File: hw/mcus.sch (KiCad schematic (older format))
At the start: 45 parts, among them P14 CONN_2, P18 CONN_1, SW2 EVQP7A01K, U10 MICRON N25Q032A13ESC40G, U13 MPU-9250, U7 STM32F427VIT6, U8 STM32F303CC, U9 MS5611, X1 8MHz, X2 8MHz

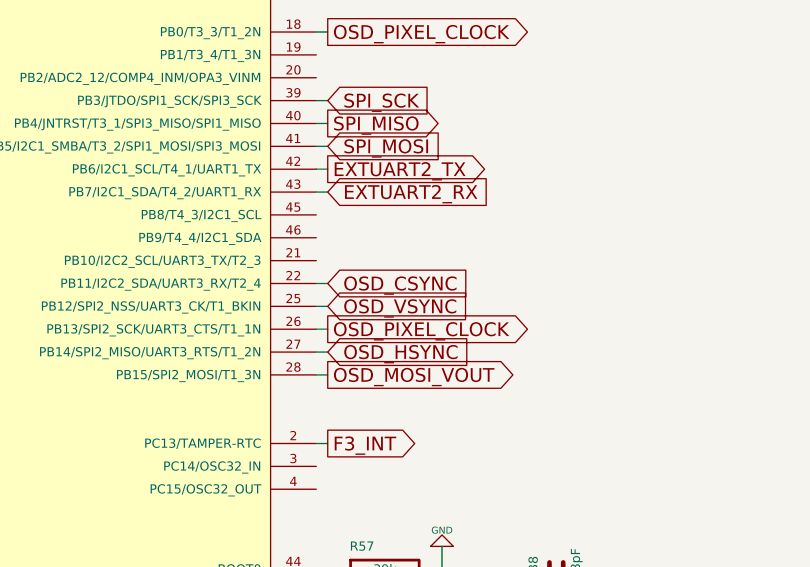
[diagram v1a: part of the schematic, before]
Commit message: hw: add chroma filter to sync separator, removed unused CSYNC signal
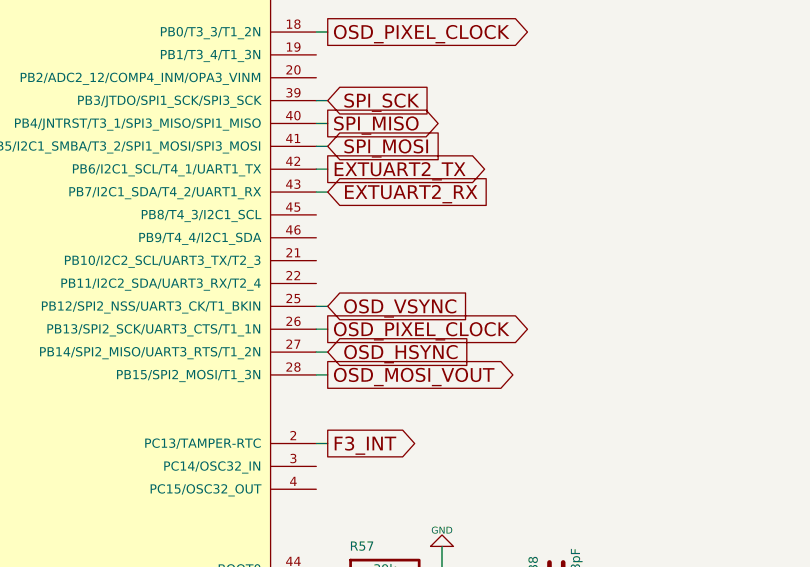
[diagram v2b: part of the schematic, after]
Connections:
- net OSD_CSYNC: no longer names the net of U8.22 (PB11/I2C2_SDA/UART3_RX/T2_4)
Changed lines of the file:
@@
 Text GLabel 9750 3300 2    60   Input ~ 0
 OSD_HSYNC
-Text GLabel 9750 3000 2    60   Input ~ 0
-OSD_CSYNC
 Wire Wire Line
 	9700 3300 9750 3300
@@
 	1800 6450 1850 6450
 Wire Wire Line
-	9700 3000 9750 3000
-Wire Wire Line
 	6650 2500 6700 2500
